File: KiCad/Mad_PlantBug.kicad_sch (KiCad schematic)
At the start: 35 parts, among them IC1 TMP102AIDRLR, J2 Conn_01x03, Q1 AO3401A, Q2 YJL2302B, U1 YJ-14015, U2 TLV333IDBVR

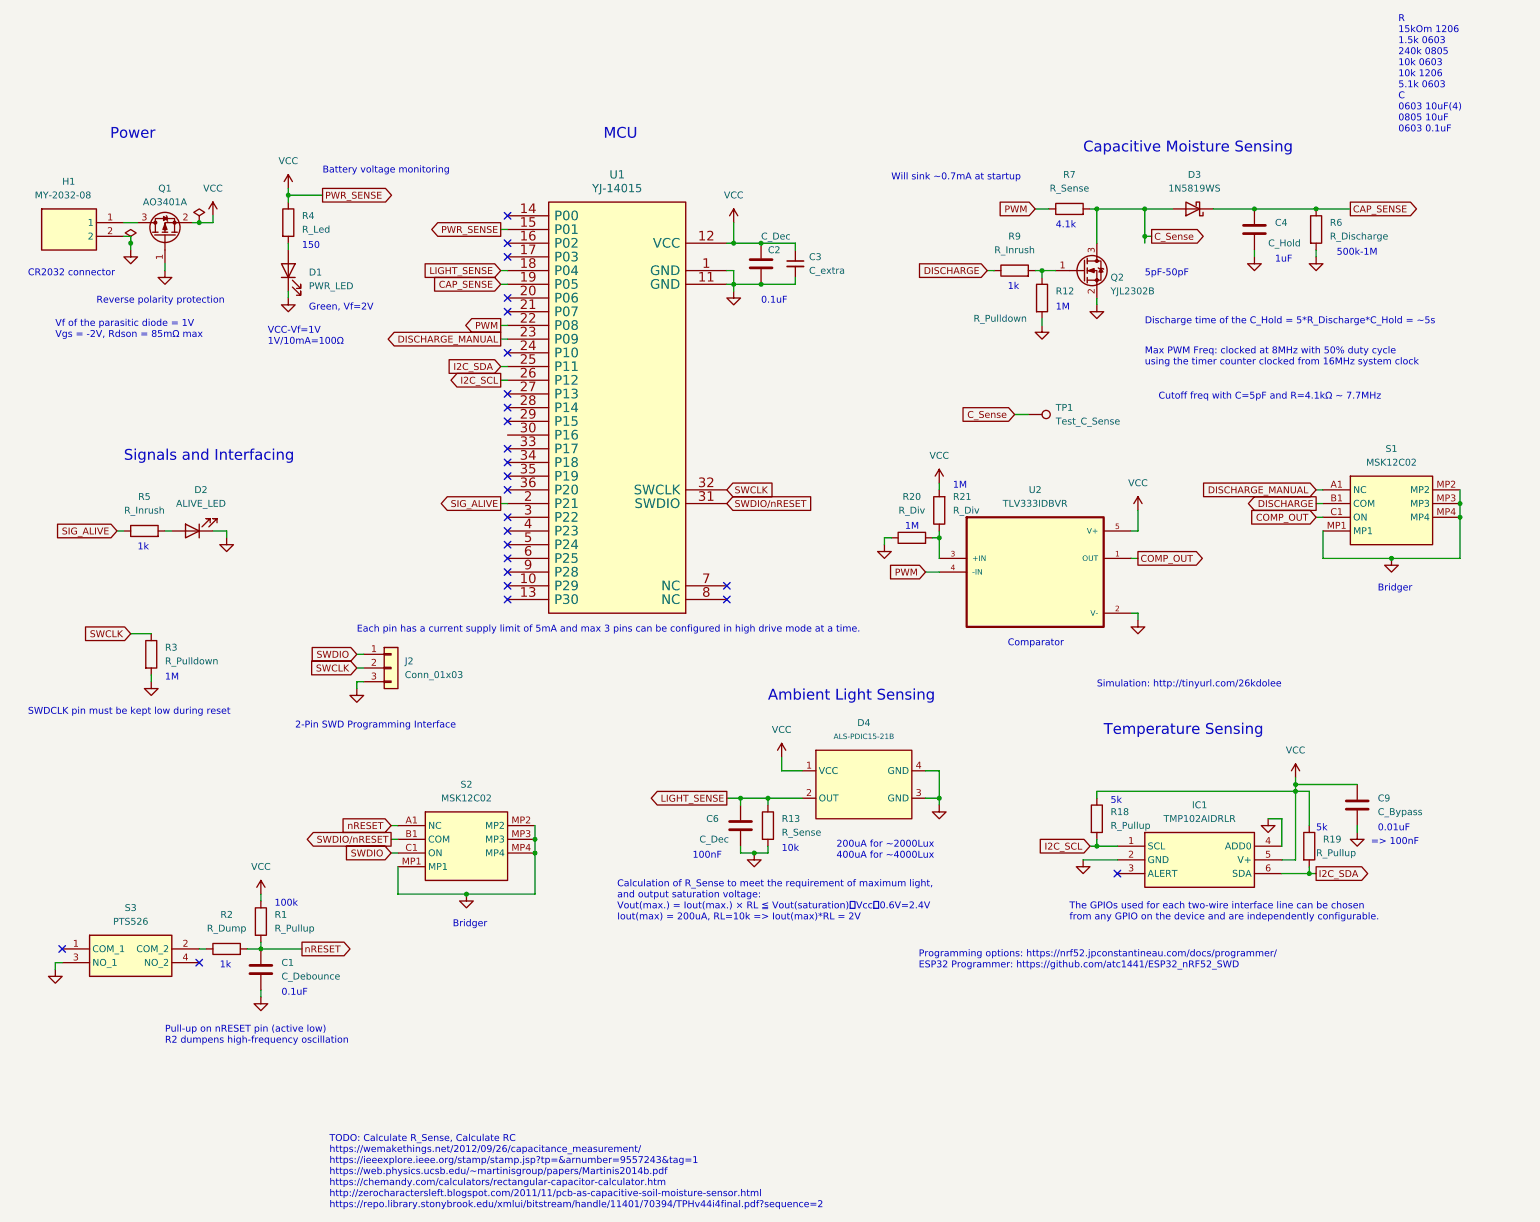
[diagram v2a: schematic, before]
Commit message: Routed UART, added some designators, added gerbers.
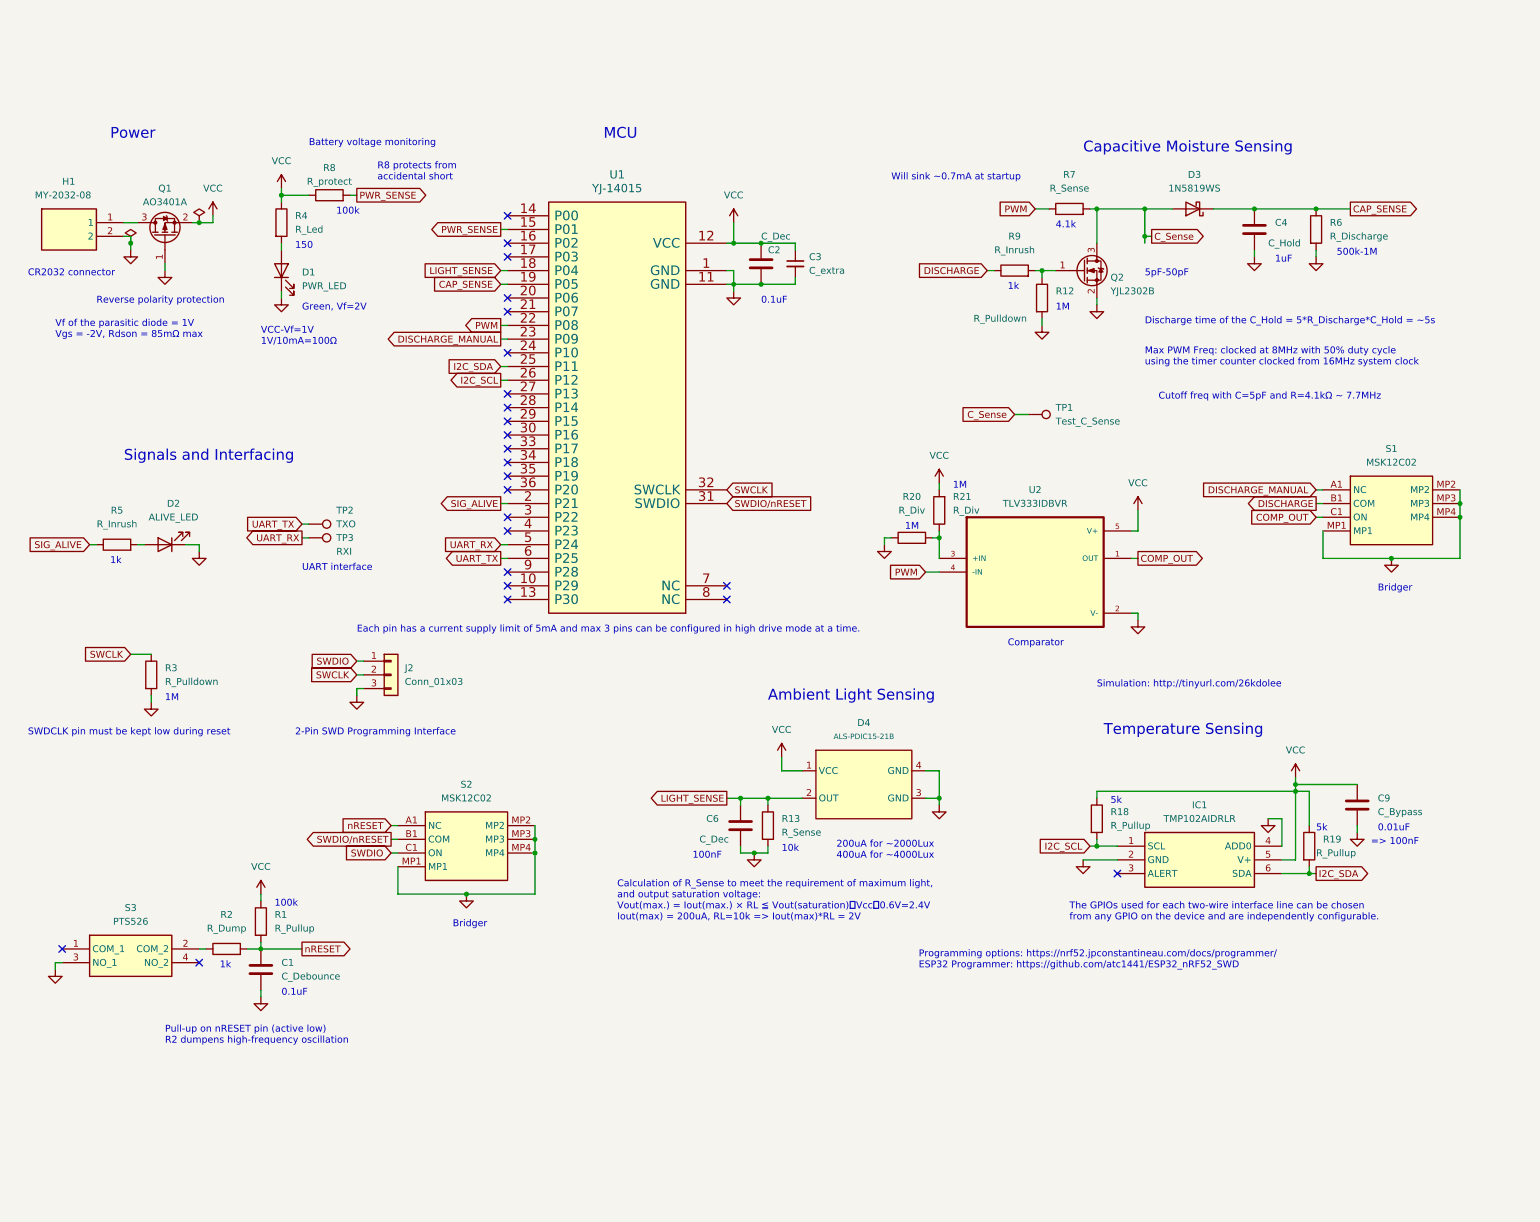
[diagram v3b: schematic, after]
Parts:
- added R8: R_protect, Resistor_SMD:R_0402_1005Metric_Pad0.72x0.64mm_HandSolder, symbol Device:R
- added TP2: TXO, TestPoint:TestPoint_Pad_1.0x1.0mm, symbol Connector:TestPoint
- added TP3: RXI, TestPoint:TestPoint_Pad_1.0x1.0mm, symbol Connector:TestPoint
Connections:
- net VCC: now also R8.1; no longer U1.15 (P01)
- net UART_RX: now reaches U1.5 (P24)
- net UART_RX: now also TP3.1
- net UART_TX: now reaches U1.6 (P25)
- net UART_TX: now also TP2.1
- new net PWR_SENSE: R8.2, U1.15 (P01)
- no-connect marks 25 -> 24
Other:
- note added: "R8 protects from accidental short"
- note added: "UART interface"
- note removed: "R 15kOm 1206 1.5k 0603 240k 0805 10k 0603 10k 1206 5.1k 0603 C 0603 10uF(4) 0805 10uF 0603 0.1uF"
- note removed: "TODO: Calculate R_Sense, Calculate RC https://wemakethings.net/2012/09/26/capacitance_measurement/ https://ieeexplore.ieee.org/stamp/stamp.jsp?tp=&arnumber=9557243&tag=1 https://web.physics.ucsb.edu/~martinisgroup/papers/Martinis2014b.pdf https://chemandy.com/calculators/rectangular-capacitor-calculator.htm http://zerocharactersleft.blogspot.com/2011/11/pcb-as-capacitive-soil-moisture-sensor.html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"
- moved on the sheet: D1, D2, J2, R3, R4, R5
